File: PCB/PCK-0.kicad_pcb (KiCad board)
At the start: 2 copper layers, 102 parts, among them J1 USB_C_Receptacle_USB2.0_16P, J2 BAT+, J3 BAT-, SW1 EN, SW10 5, SW11 M2, SW12 TAB, SW13 Q, SW14 W, SW15 E, SW16 R, SW17 T, SW18 M3, SW19 CAPSLOCK, SW2 BOOT, SW20 A, SW21 S, SW22 D, SW23 F, SW24 G, SW25 M4, SW26 LSHIFT, SW27 Z, SW28 X, SW29 C, SW3 RotaryEncoder_Switch_MP, SW30 V, SW31 SPACE, SW32 M5, SW33 FN, SW34 CTRL, SW35 SUPER, SW36 ALT, SW37 MOD1, SW38 MOD2, SW4 M1, SW5 ESC, SW6 1, SW7 2, SW8 3, SW9 4, U1 NCP1117-3.3_SOT223, U2 NCP1117-3.3_SOT223, U3 USBLC6-2SC6, U4 ESP32-C6-MINI-1, U5 TVS1400DRV

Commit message: pcb start
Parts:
- SW10: renamed from SW12; value TAB -> 2,2
- SW11: renamed from SW19; value CAPSLOCK -> 2,3
- SW12: renamed from SW26; value LSHIFT -> 2,4
- SW13: renamed from SW33; value FN -> 2,5
- SW14: renamed from SW6; value 1 -> 3,1
- SW15: renamed from SW13; value Q -> 3,2
- SW16: renamed from SW20; value A -> 3,3
- SW17: renamed from SW27; value Z -> 3,4
- SW18: renamed from SW34; value CTRL -> 3,5
- SW19: renamed from SW7; value 2 -> 4,1
- SW20: renamed from SW14; value W -> 4,2
- SW21: value S -> 4,3
- SW22: renamed from SW28; value X -> 4,4
- SW23: renamed from SW35; value SUPER -> 4,5
- SW24: renamed from SW8; value 3 -> 5,1
- SW25: renamed from SW15; value E -> 5,2
- SW26: renamed from SW22; value D -> 5,3
- SW27: renamed from SW29; value C -> 5,4
- SW28: renamed from SW36; value ALT -> 5,5
- SW29: renamed from SW9; value 4 -> 6,1
- SW30: renamed from SW16; value R -> 6,2
- SW31: renamed from SW23; value F -> 6,3
- SW32: renamed from SW30; value V -> 6,4
- SW33: renamed from SW37; value MOD1 -> 6,5
- SW34: renamed from SW10; value 5 -> 7,1
- SW35: renamed from SW17; value T -> 7,2
- SW36: renamed from SW24; value G -> 7,3
- SW37: renamed from SW31; value SPACE -> 7,4
- SW38: value MOD2 -> 7,5
- SW4: value M1 -> 1,1
- SW5: renamed from SW11; value M2 -> 1,2
- SW6: renamed from SW18; value M3 -> 1,3
- SW7: renamed from SW25; value M4 -> 1,4
- SW8: renamed from SW32; value M5 -> 1,5
- SW9: renamed from SW5; value ESC -> 2,1
- moved SW24 85.4 mm to (84.4, 16.4)
- moved SW18 85.4 mm to (54.2, 76.8)
- moved SW8 77.0 mm to (24.0, 76.8)
- moved SW34 76.9 mm to (114.6, 16.4)
- moved SW7 67.5 mm to (24.0, 61.7)
- moved SW35 67.5 mm to (114.6, 31.5)
- moved SW19 64.0 mm to (69.3, 16.4)
- moved SW23 64.0 mm to (69.3, 76.8)
- moved SW13 60.4 mm to (39.1, 76.8)
- moved SW29 60.3 mm to (99.5, 16.4)
- moved SW15 47.7 mm to (54.2, 31.5)
- moved SW12 47.7 mm to (39.1, 61.7)
- moved SW30 47.7 mm to (99.5, 31.5)
- moved SW27 47.7 mm to (84.4, 61.7)
- moved SW6 42.7 mm to (24.0, 46.6)
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- renumbered C6 to C4, C4 to C5, C5 to C6, H3 to H2, H2 to H3, R6 to R3, R7 to R4, R3 to R5, R4 to R6, R5 to R7, SW3 to SW1, SW1 to SW2, SW2 to SW3, U5 to U2, U2 to U3, U3 to U4, U4 to U5
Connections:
- D10 pad 1: /IO20 -> /IO21
- D11 pad 1: /IO20 -> /IO22
- D12 pad 1: /IO20 -> /IO23
- D13 pad 1: /IO20 -> /IO19
- D15 pad 1: /IO20 -> /IO21
- D16 pad 1: /IO20 -> /IO22
- D17 pad 1: /IO21 -> /IO23
- D18 pad 1: /IO21 -> /IO19
- D19 pad 1: /IO21 -> /IO20
- D21 pad 1: /IO21 -> /IO22
- D22 pad 1: /IO21 -> /IO23
- D23 pad 1: /IO21 -> /IO19
- D24 pad 1: /IO22 -> /IO20
- D25 pad 1: /IO22 -> /IO21
- D27 pad 1: /IO22 -> /IO23
- D28 pad 1: /IO22 -> /IO19
- D29 pad 1: /IO22 -> /IO20
- D30 pad 1: /IO22 -> /IO21
- D31 pad 1: /IO23 -> /IO22
- D33 pad 1: /IO23 -> /IO19
- D34 pad 1: /IO23 -> /IO20
- D35 pad 1: /IO23 -> /IO21
- D36 pad 1: /IO23 -> /IO22
- D4 pad 1: /IO19 -> /IO20
- D5 pad 1: /IO19 -> /IO21
- D6 pad 1: /IO19 -> /IO22
- D7 pad 1: /IO19 -> /IO23
- D9 pad 1: /IO19 -> /IO20
- SW10 pad 2: Net-(D11-A) -> Net-(D9-A)
- SW11 pad 2: Net-(D18-A) -> Net-(D10-A)
- SW12 pad 2: Net-(D25-A) -> Net-(D11-A)
- SW13 pad 2: Net-(D32-A) -> Net-(D12-A)
- SW14 pad 2: Net-(D5-A) -> Net-(D13-A)
- SW15 pad 2: Net-(D12-A) -> Net-(D14-A)
- SW16 pad 2: Net-(D19-A) -> Net-(D15-A)
- SW17 pad 2: Net-(D26-A) -> Net-(D16-A)
- SW18 pad 2: Net-(D33-A) -> Net-(D17-A)
- SW19 pad 2: Net-(D6-A) -> Net-(D18-A)
- SW20 pad 2: Net-(D13-A) -> Net-(D19-A)
- SW22 pad 2: Net-(D27-A) -> Net-(D21-A)
- SW23 pad 2: Net-(D34-A) -> Net-(D22-A)
- SW24 pad 2: Net-(D7-A) -> Net-(D23-A)
- SW25 pad 2: Net-(D14-A) -> Net-(D24-A)
- SW26 pad 2: Net-(D21-A) -> Net-(D25-A)
- SW27 pad 2: Net-(D28-A) -> Net-(D26-A)
- SW28 pad 2: Net-(D35-A) -> Net-(D27-A)
- SW29 pad 2: Net-(D8-A) -> Net-(D28-A)
- SW30 pad 2: Net-(D15-A) -> Net-(D29-A)
- SW31 pad 2: Net-(D22-A) -> Net-(D30-A)
- SW32 pad 2: Net-(D29-A) -> Net-(D31-A)
- SW33 pad 2: Net-(D36-A) -> Net-(D32-A)
- SW34 pad 2: Net-(D9-A) -> Net-(D33-A)
- SW35 pad 2: Net-(D16-A) -> Net-(D34-A)
- SW36 pad 2: Net-(D23-A) -> Net-(D35-A)
- SW37 pad 2: Net-(D30-A) -> Net-(D36-A)
- SW5 pad 2: Net-(D10-A) -> Net-(D4-A)
- SW6 pad 2: Net-(D17-A) -> Net-(D5-A)
- SW7 pad 2: Net-(D24-A) -> Net-(D6-A)
- SW8 pad 2: Net-(D31-A) -> Net-(D7-A)
- SW9 pad 2: Net-(D4-A) -> Net-(D8-A)

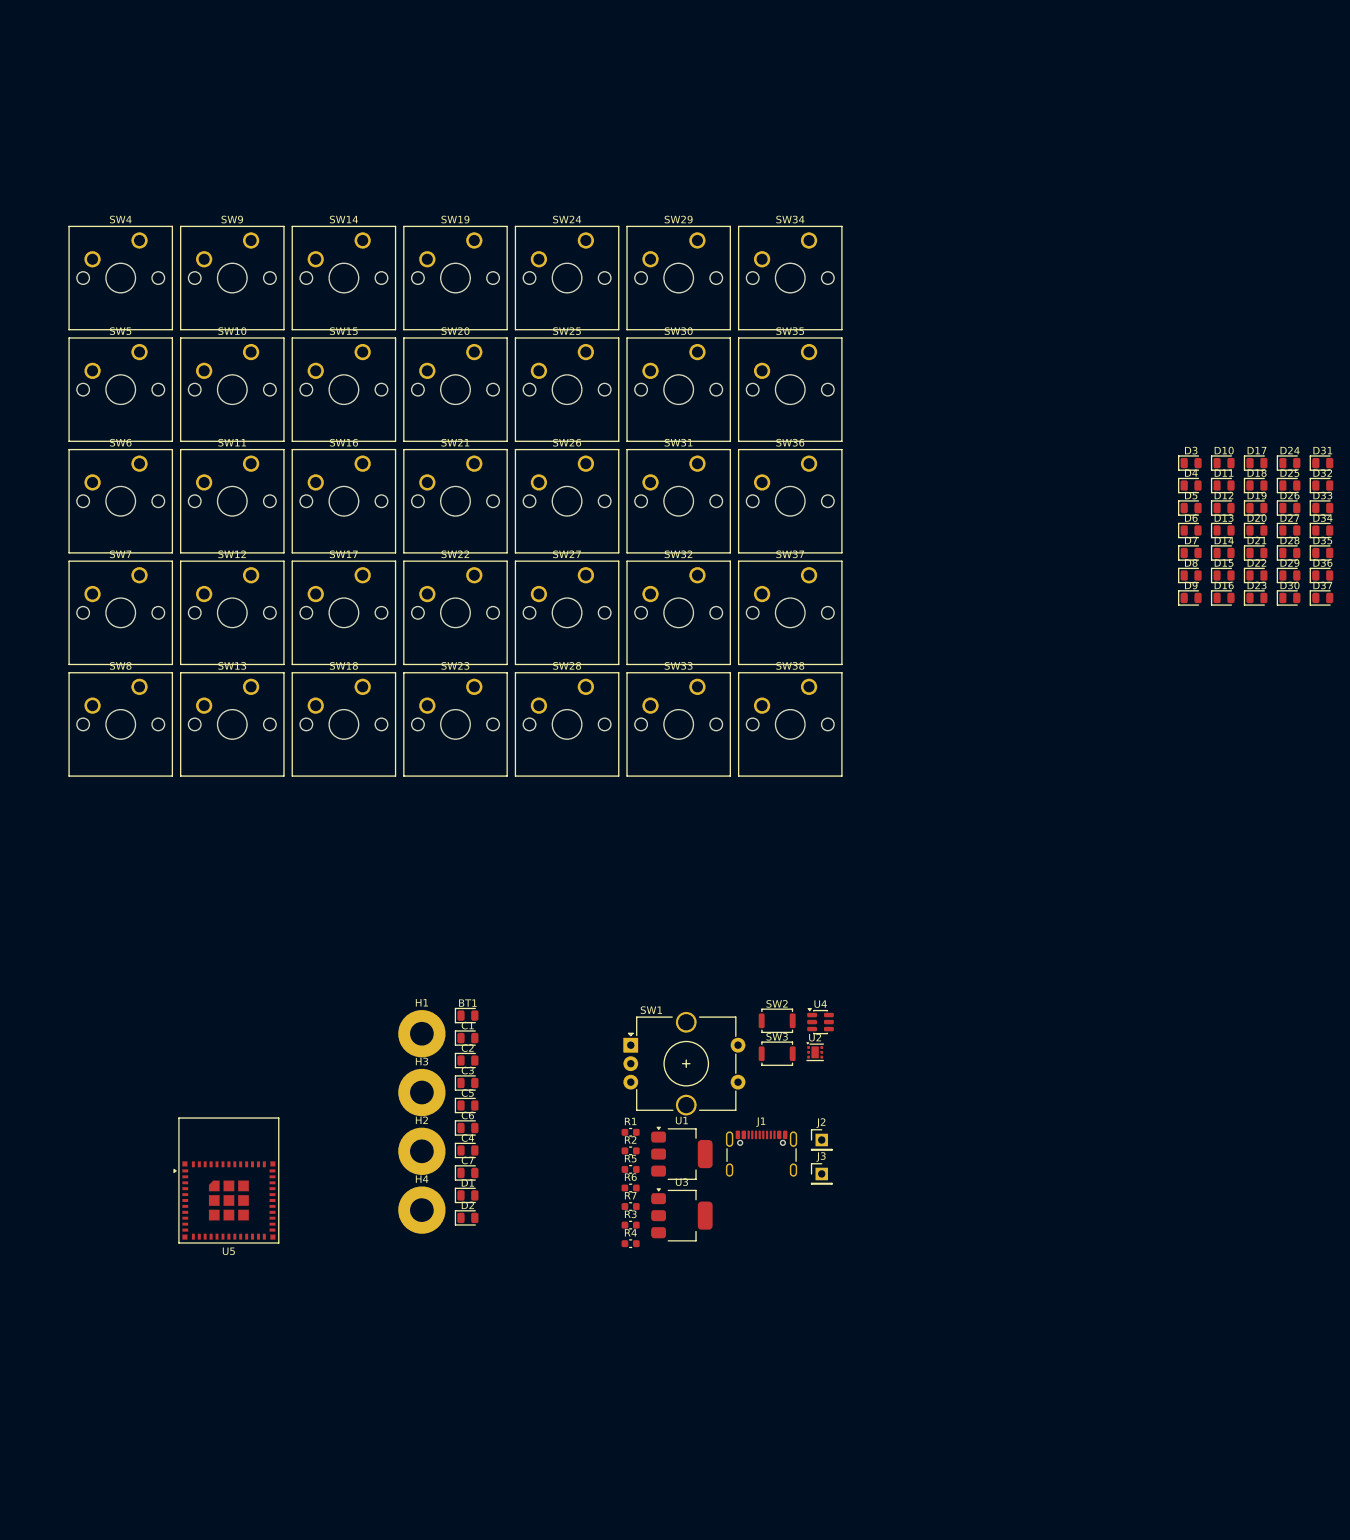
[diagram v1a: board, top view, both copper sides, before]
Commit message: pcb key layout done
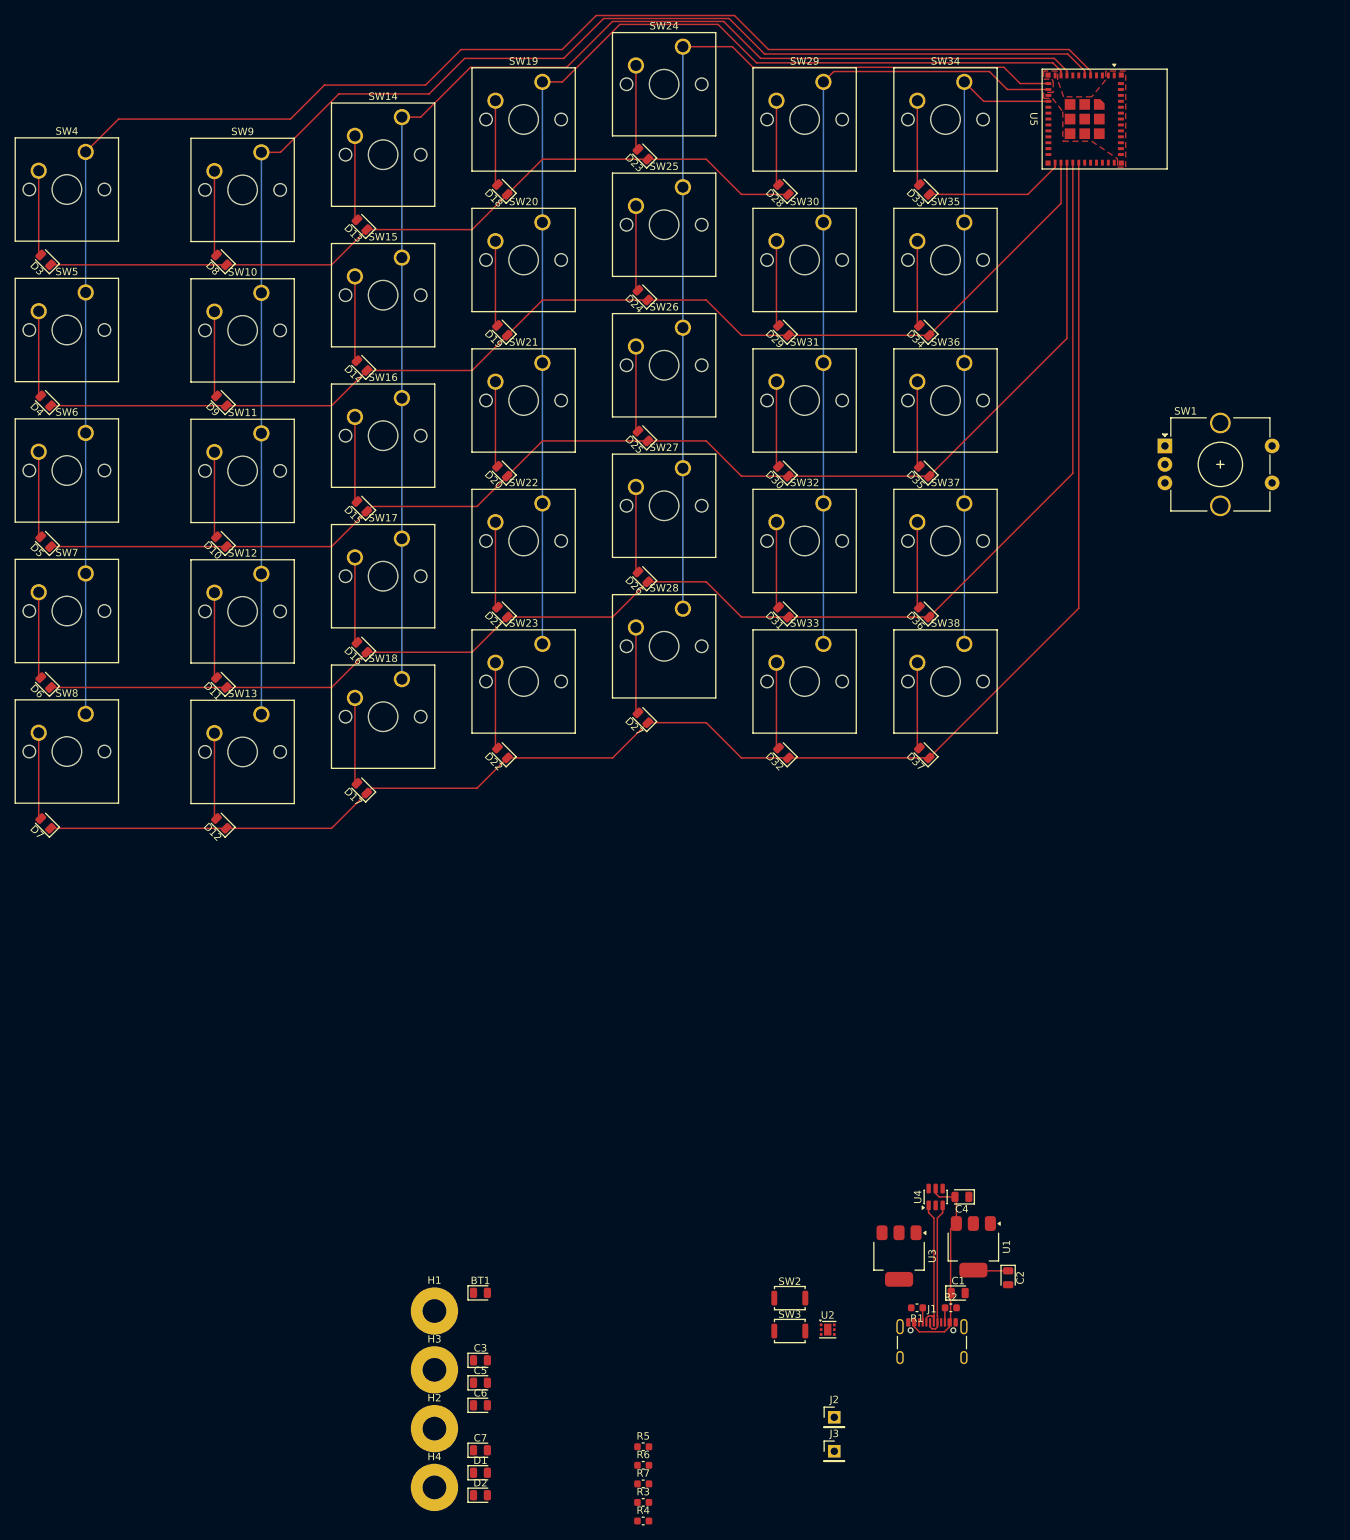
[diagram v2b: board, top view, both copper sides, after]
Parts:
- SW4, SW5, SW6, SW7, SW8: footprint Button_Switch_Keyboard:SW_Cherry_MX_1.00u_PCB -> Button_Switch_Keyboard:SW_Cherry_MX_1.50u_PCB
- moved U5 186.5 mm to (151.8, 0.00), turned to -90 degrees
- moved D7 159.2 mm to (11.3, 95.2), turned to 135 degrees
- moved D3 157.3 mm to (11.3, 19.1), turned to 135 degrees
- moved D6 156.3 mm to (11.3, 76.2), turned to 135 degrees
- moved D4 155.3 mm to (11.3, 38.1), turned to 135 degrees
- moved D5 155.0 mm to (11.3, 57.1), turned to 135 degrees
- moved D12 142.1 mm to (35.1, 95.2), turned to 135 degrees
- moved D11 138.2 mm to (35.1, 76.2), turned to 135 degrees
- moved D8 137.9 mm to (35.1, 19.1), turned to 135 degrees
- moved D10 136.0 mm to (35.1, 57.1), turned to 135 degrees
- moved D9 133.8 mm to (35.1, 38.1), turned to 135 degrees
- moved D17 128.8 mm to (54.1, 90.5), turned to 135 degrees
- moved D13 123.7 mm to (54.1, 14.3), turned to 135 degrees
- moved D14 119.3 mm to (54.1, 33.3), turned to 135 degrees
- moved D15 117.0 mm to (54.1, 52.4), turned to 135 degrees
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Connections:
- SW10 pad 1: /IO1 -> /IO3
- SW11 pad 1: /IO1 -> /IO3
- SW12 pad 1: /IO1 -> /IO3
- SW13 pad 1: /IO1 -> /IO3
- SW14 pad 1: /IO2 -> /IO4
- SW15 pad 1: /IO2 -> /IO4
- SW16 pad 1: /IO2 -> /IO4
- SW17 pad 1: /IO2 -> /IO4
- SW18 pad 1: /IO2 -> /IO4
- SW19 pad 1: /IO3 -> /IO5
- SW20 pad 1: /IO3 -> /IO5
- SW21 pad 1: /IO3 -> /IO5
- SW22 pad 1: /IO3 -> /IO5
- SW23 pad 1: /IO3 -> /IO5
- SW24 pad 1: /IO4 -> /IO0
- SW25 pad 1: /IO4 -> /IO0
- SW26 pad 1: /IO4 -> /IO0
- SW27 pad 1: /IO4 -> /IO0
- SW28 pad 1: /IO4 -> /IO0
- SW29 pad 1: /IO5 -> /IO1
- SW30 pad 1: /IO5 -> /IO1
- SW31 pad 1: /IO5 -> /IO1
- SW32 pad 1: /IO5 -> /IO1
- SW33 pad 1: /IO5 -> /IO1
- SW4 pad 1: /IO0 -> /IO2
- SW5 pad 1: /IO0 -> /IO2
- SW6 pad 1: /IO0 -> /IO2
- SW7 pad 1: /IO0 -> /IO2
- SW8 pad 1: /IO0 -> /IO2
- SW9 pad 1: /IO1 -> /IO3
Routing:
- net /IO2: track 0.00 -> 223.2 mm
- net /IO23: track 0.00 -> 215.6 mm
- net /IO3: track 0.00 -> 198.4 mm
- net /IO22: track 0.00 -> 196.2 mm
- net /IO21: track 0.00 -> 176.8 mm
- net /IO4: track 0.00 -> 174.7 mm
- net /IO20: track 0.00 -> 157.4 mm
- net /IO5: track 0.00 -> 152.6 mm
- net /IO0: track 0.00 -> 127.5 mm
- net /IO19: track 0.00 -> 126.8 mm
- net /IO1: track 0.00 -> 108.0 mm
- net /IO6: track 0.00 -> 88.5 mm
- net VBUS: track 0.00 -> 27.4 mm
- net /D-: track 0.00 -> 18.6 mm
- net /D+: track 0.00 -> 18.6 mm
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- added copper zone on F.Cu, net GND

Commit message: key layout rework
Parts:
- D10, D11, D12, D13, D14, D15, D16, D17, D18, D19, D20, D21, D22, D23, D24, D25, D26, D27, D28, D29, D3, D30, D31, D32, D33, D34, D35, D36, D37, D4, D5, D6, D7, D8, D9: moved to B.Cu
- SW33: footprint Button_Switch_Keyboard:SW_Cherry_MX_1.00u_PCB -> Button_Switch_Keyboard:SW_Cherry_MX_1.75u_PCB
- moved BT1 511.1 mm to (-373.2, 412.9)
- moved R6 511.1 mm to (-351.2, 436.3)
- moved U4 511.1 mm to (-311.7, 400.0)
- moved C1 511.1 mm to (-308.6, 413.0)
- moved C2 511.1 mm to (-301.9, 410.9)
- moved C3 511.1 mm to (-373.2, 422.1)
- moved C4 511.1 mm to (-308.1, 400.0)
- moved C5 511.1 mm to (-373.2, 425.1)
- moved C6 511.1 mm to (-373.2, 428.1)
- moved C7 511.1 mm to (-373.2, 434.2)
- moved D1 511.1 mm to (-373.2, 437.3)
- moved D2 511.1 mm to (-373.2, 440.3)
- moved H1 511.1 mm to (-379.4, 415.4)
- moved H2 511.1 mm to (-379.4, 431.3)
- moved H3 511.1 mm to (-379.4, 423.3)
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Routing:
- net /IO2: track 223.2 -> 76.2 mm
- net /IO3: track 198.4 -> 76.2 mm
- net /IO23: track 215.6 -> 108.3 mm
- net /IO4: track 174.7 -> 76.2 mm
- net /IO22: track 196.2 -> 98.8 mm
- net /IO21: track 176.8 -> 98.8 mm
- net /IO5: track 152.6 -> 76.2 mm
- net /IO20: track 157.4 -> 98.8 mm
- net /IO0: track 127.5 -> 76.2 mm
- net /IO1: track 108.0 -> 79.2 mm
- net /IO19: track 126.8 -> 98.8 mm
- net /IO6: track 88.5 -> 106.9 mm
- net Net-(D37-A): track 11.7 -> 0.00 mm
- net Net-(D36-A): track 11.6 -> 0.00 mm
- net Net-(D35-A): track 11.6 -> 0.00 mm
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- removed copper zone on F.Cu, net GND

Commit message: ground plane and some power routing
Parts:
- moved BT1 702.9 mm to (230.3, 52.7)
- moved C6 702.9 mm to (230.3, 67.9)
- moved C7 702.9 mm to (230.3, 74.0)
- moved H1 702.9 mm to (224.1, 55.1)
- moved H2 702.9 mm to (224.1, 71.0)
- moved H3 702.9 mm to (224.1, 63.1)
- moved J2 702.9 mm to (278.2, 69.5)
- moved J3 702.9 mm to (278.2, 74.1)
- moved R5 702.9 mm to (252.4, 73.5)
- moved R6 702.9 mm to (252.4, 76.0)
- moved R7 702.9 mm to (252.4, 78.5)
- moved H4 702.9 mm to (224.1, 79.0)
- moved C3 663.0 mm to (167.5, 38.4)
- moved C5 658.7 mm to (163.0, 42.6), turned to -90 degrees
- moved D2 657.9 mm to (162.6, 58.6), turned to 180 degrees
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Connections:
- U5 pad 17: /IO12 -> /USB_D-
- U5 pad 18: /IO13 -> /USB_D+
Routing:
- net +3V3: track 4.74 -> 88.3 mm
- net /USB_D+: track 0.00 -> 22.0 mm
- net /USB_D-: track 0.00 -> 22.0 mm
- net /IO22: track 98.8 -> 119.6 mm
- net Net-(D36-A): track 0.00 -> 20.3 mm, vias 0 -> 1
- net Net-(U5-EN): track 0.00 -> 14.3 mm, vias 0 -> 2
- net Net-(D37-A): track 0.00 -> 11.5 mm
- net /IO23: track 108.3 -> 114.6 mm
- net VBAT: track 0.00 -> 6.28 mm
- net Net-(D33-A): track 0.00 -> 5.92 mm
- net /IO9: track 0.00 -> 5.25 mm
- net /IO8: track 0.00 -> 3.56 mm
- net Net-(D34-A): track 0.00 -> 2.72 mm
- net Net-(D2-A): track 0.00 -> 1.55 mm
- net Net-(D1-A): track 0.00 -> 1.52 mm
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- added copper zone on F.Cu, net GND
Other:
- board outline added: 173.1 x 128.2 mm

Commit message: mcu placement rework, power zones
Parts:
- BT1: footprint Diode_SMD:D_0805_2012Metric -> Battery:BatteryHolder_Keystone_1042_1x18650; moved to B.Cu
- J2: moved to B.Cu
- moved D2 331.7 mm to (484.1, 140.4), turned to 0 degrees
- moved D1 331.4 mm to (484.1, 137.4), turned to 0 degrees
- moved R4 315.7 mm to (465.6, 135.5), turned to 0 degrees
- moved R3 315.5 mm to (465.6, 133.0), turned to 0 degrees
- moved H3 273.8 mm to (493.2, 113.7)
- moved H1 272.5 mm to (493.2, 97.8)
- moved H4 272.5 mm to (493.2, 121.7)
- moved H2 271.3 mm to (493.2, 105.8)
- moved BT1 192.6 mm to (418.5, 93.8), turned to -90 degrees
- moved C2 170.8 mm to (311.7, 60.3), turned to -90 degrees
- moved U5 165.9 mm to (337.8, 52.1), turned to 0 degrees
- moved U1 164.7 mm to (311.7, 54.0), turned to -90 degrees
- moved U3 162.1 mm to (319.0, 54.0), turned to -90 degrees
- moved C1 161.4 mm to (310.3, 48.5), turned to 0 degrees
- moved C5 157.0 mm to (319.0, 60.2)
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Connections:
- J1 pad SH: Earth_Protective -> GND
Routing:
- net +3V3: track 88.3 -> 12.6 mm
- net /USB_D+: track 22.0 -> 37.8 mm
- net /USB_D-: track 22.0 -> 36.7 mm
- net Net-(U5-EN): track 14.3 -> 1.15 mm, vias 2 -> 1
- net VBUS: track 27.4 -> 15.2 mm
- net /D-: track 18.6 -> 10.8 mm
- net /D+: track 18.6 -> 11.2 mm
- net /IO9: track 5.25 -> 0.00 mm
- net /IO8: track 3.56 -> 0.00 mm
- net /IO7: track 1.07 -> 3.66 mm
- net Net-(D2-A): track 1.55 -> 0.00 mm
- net Net-(D1-A): track 1.52 -> 0.00 mm
- net /IO15: track 1.47 -> 0.00 mm, vias 1 -> 0
- net /IO14: track 1.47 -> 0.00 mm, vias 1 -> 0
- net /IO1: track 80.3 -> 81.8 mm
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- added copper zone on F.Cu, net +3V3
- added copper zone on F.Cu, net Earth_Protective
- added copper zone on F.Cu, net VBAT
- added copper zone on F.Cu, net VBUS
- removed copper zone on F.Cu, net GND
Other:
- board size 173.1 x 128.2 mm -> 328.9 x 128.2 mm
